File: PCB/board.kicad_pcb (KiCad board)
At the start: 2 copper layers, 81.7 x 88.8 mm, 161 parts, among them J1 Micro_SD_Card, J10 Conn_01x10, J11 Conn_01x02, J12 Conn_02x04_Odd_Even, J13 Conn_01x02, J14 Conn_01x02, J15 Conn_01x03, J16 Conn_01x02, J17 Conn_01x05, J18 Conn_01x04, J19 Conn_01x04, J2 Conn_ARM_JTAG_SWD_10, J20 Conn_01x02, J21 Conn_01x03, J22 Conn_02x04_Odd_Even, J23 Conn_01x04, J24 Conn_01x04, J25 Conn_01x02, J26 Conn_01x03, J27 Conn_02x04_Odd_Even, J28 Conn_01x04, J29 Conn_01x04, J3 USB_C_Receptacle_USB2.0_14P, J30 Conn_01x02, J31 Conn_01x03, J32 Conn_01x02, J33 Conn_01x02, J34 Conn_01x02, J35 Conn_01x02, J36 Conn_01x02, J37 Conn_01x02, J4 Conn_01x04, J5 Conn_01x04, J6 Conn_01x02, J7 Conn_01x03, J8 Conn_02x04_Odd_Even, J9 Conn_01x10, Q1 IRLML6402, Q2 NMOS, Q3 NMOS, Q4 NMOS, Q5 Q_NMOS_GDS, Q7 Q_NMOS_GDS, SW1 SW_Push, SW2 SW_Push, U1 STM32H743VITx, U2 AP7361C, U4 TMC Stepstick, U5 TMC Stepstick, U6 TMC Stepstick, U7 TMC Stepstick, U8 AP63203WU, Y2 25 MHz

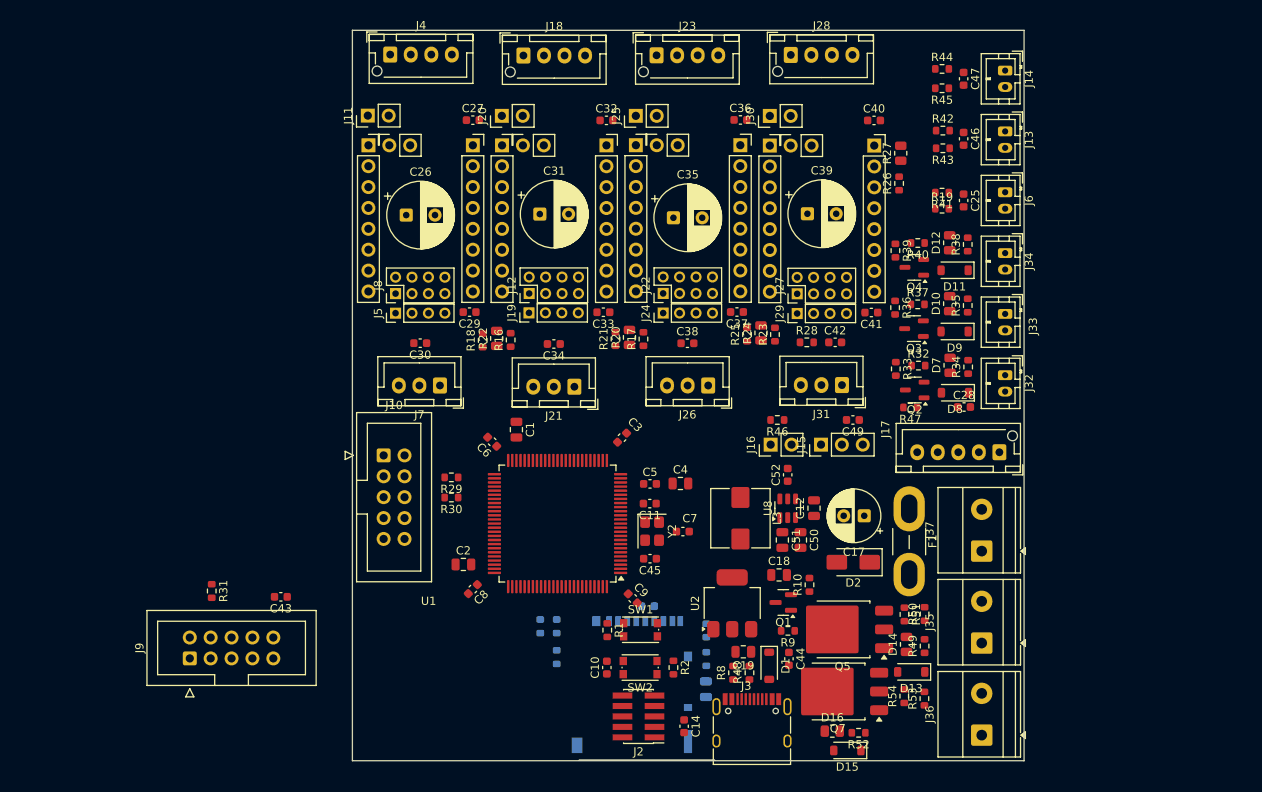
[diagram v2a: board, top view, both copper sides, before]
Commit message: first round of mounting holes
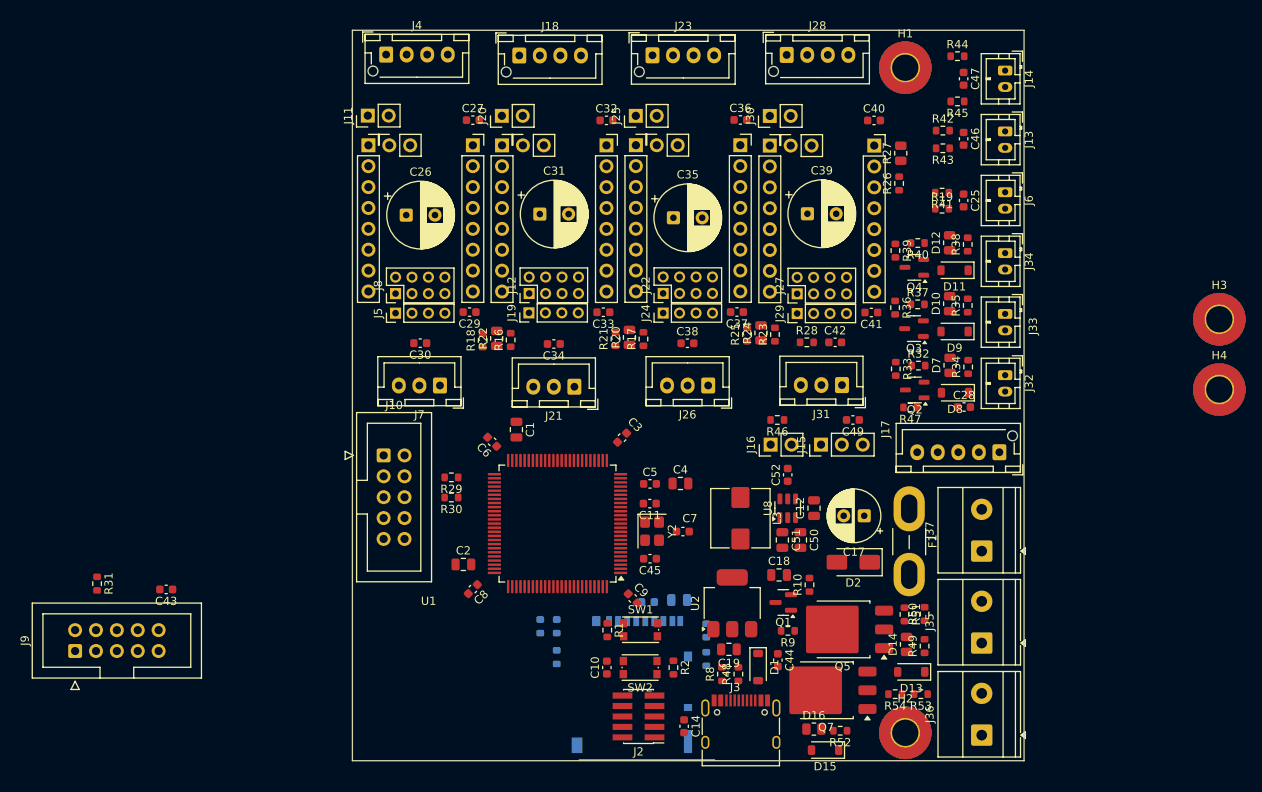
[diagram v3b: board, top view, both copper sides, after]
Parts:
- added H1: MountingHole_Pad, MountingHole:MountingHole_3.2mm_M3_Pad_TopBottom, F.Cu at (220.8, 28.5)
- added H2: MountingHole_Pad, MountingHole:MountingHole_3.2mm_M3_Pad_TopBottom, F.Cu at (220.8, 109.4)
- added H3: MountingHole_Pad, MountingHole:MountingHole_3.2mm_M3_Pad_TopBottom, F.Cu at (259.0, 59.1)
- added H4: MountingHole_Pad, MountingHole:MountingHole_3.2mm_M3_Pad_TopBottom, F.Cu at (259.0, 67.7)
- moved J9 14.0 mm to (119.8, 99.5)
- moved R31 14.0 mm to (122.5, 91.3)
- moved C43 14.0 mm to (130.9, 92.0)
- moved C16 11.3 mm to (193.3, 93.2), turned to 0 degrees
- moved D15 2.70 mm to (211.1, 111.5)
- moved R45 2.46 mm to (227.2, 32.6)
- moved R44 2.43 mm to (227.2, 27.1)
- moved D16 2.25 mm to (209.7, 109.0)
- moved R52 2.25 mm to (212.9, 109.2)
- moved C19 1.78 mm to (199.3, 99.2)
- moved Q7 1.43 mm to (211.2, 104.2)
- moved J3 1.36 mm to (200.8, 109.5)
- moved R48 1.36 mm to (200.5, 102.3)
- moved R8 1.36 mm to (198.5, 102.3)
- moved C44 1.36 mm to (205.3, 100.6)
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
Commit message: ALL mounting holes placed down
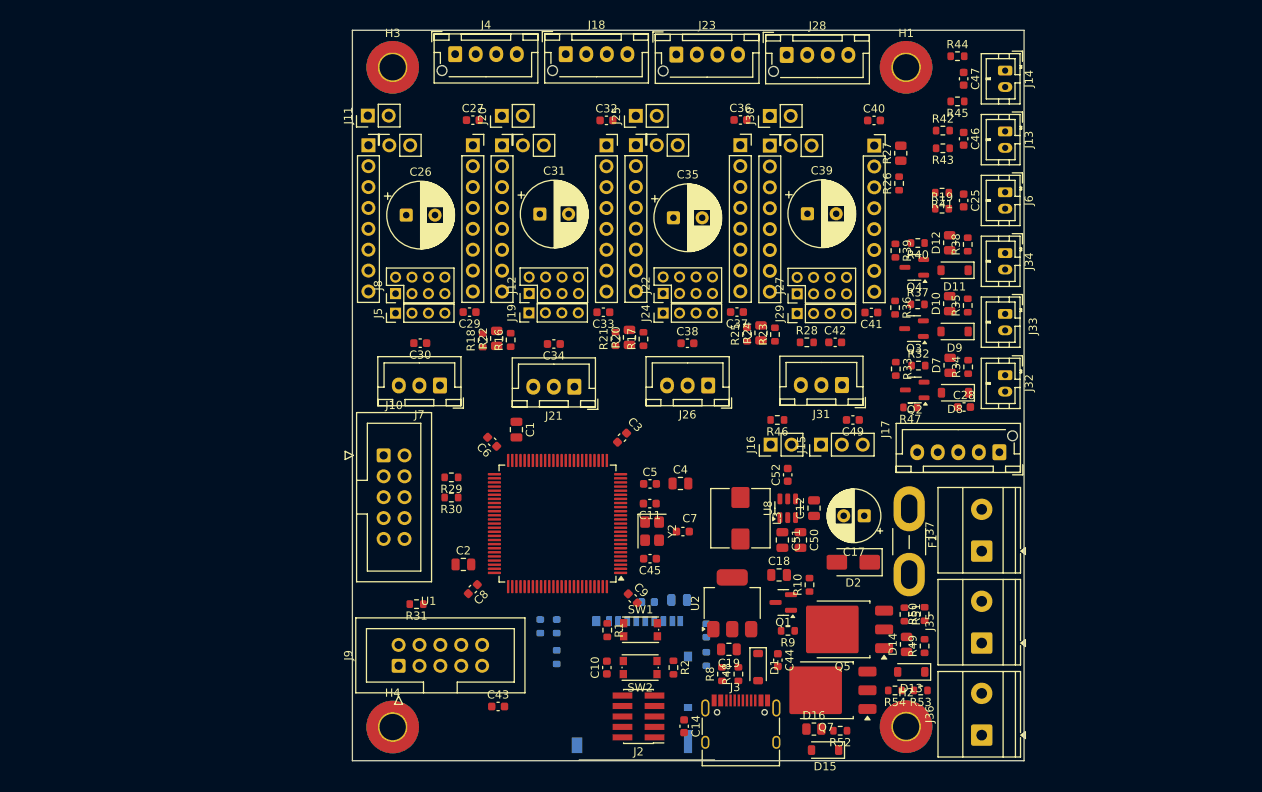
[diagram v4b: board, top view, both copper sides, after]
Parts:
- moved H4 108.6 mm to (158.4, 108.7)
- moved H3 105.1 mm to (158.4, 28.4)
- moved C43 42.8 mm to (171.3, 106.2), turned to 0 degrees
- moved J9 39.4 mm to (159.2, 101.3)
- moved R31 38.9 mm to (161.3, 93.8), turned to 180 degrees
- moved J4 8.40 mm to (166.1, 26.9)
- moved J18 5.65 mm to (179.5, 26.9)
- moved J23 2.90 mm to (192.9, 26.9)
- moved H2 0.76 mm to (220.9, 108.7)
- moved R53 0.45 mm to (222.7, 104.2)
- moved R54 0.45 mm to (219.6, 104.2)
- moved H1 0.11 mm to (220.9, 28.4)
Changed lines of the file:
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@@
 	(footprint "Connector_JST:JST_XH_B4B-XH-AM_1x04_P2.50mm_Vertical"
 		(layer "F.Cu")
-		(at 157.65 26.90375)
+		(at 166.05 26.85)
 		(descr "JST XH series connector, B4B-XH-AM, with boss (http://www.jst-mfg.com/product/pdf/eng/eXH.pdf), generated with kicad-footprint-generator")
 		(tags "connector JST XH vertical boss")
@@
 	(footprint "MountingHole:MountingHole_3.2mm_M3_Pad_TopBottom"
 		(layer "F.Cu")
-		(at 259 59.1)
+		(at 158.45 28.45)
 		(descr "Mounting Hole 3.2mm, M3, generated by kicad-footprint-generator mountinghole.py")
 		(tags "mountinghole M3")
@@
 	(footprint "MountingHole:MountingHole_3.2mm_M3_Pad_TopBottom"
 		(layer "F.Cu")
-		(at 259 67.65)
+		(at 158.45 108.7)
 		(descr "Mounting Hole 3.2mm, M3, generated by kicad-footprint-generator mountinghole.py")
 		(tags "mountinghole M3")
@@
 	(footprint "Capacitor_SMD:C_0603_1608Metric"
 		(layer "F.Cu")
-		(at 130.9 91.9625 180)
+		(at 171.275 106.2)
 		(descr "Capacitor SMD 0603 (1608 Metric), square (rectangular) end terminal, IPC-7351 nominal, (Body size source: IPC-SM-782 page 76, https://www.pcb-3d.com/wordpress/wp-content/uploads/ipc-sm-782a_amendment_1_and_2.pdf), generated with kicad-footprint-generator")
 		(tags "capacitor")
@@
 		(attr smd)
 		(fp_line
-			(start -0.14058 0.51)
-			(end 0.14058 0.51)
+			(start -0.14058 -0.51)
+			(end 0.14058 -0.51)
 			(stroke
 				(width 0.12)
@@
 		)
 		(fp_line
-			(start -0.14058 -0.51)
-			(end 0.14058 -0.51)
+			(start -0.14058 0.51)
+			(end 0.14058 0.51)
 			(stroke
 				(width 0.12)
@@
 		)
 		(fp_line
-			(start 1.48 0.73)
-			(end -1.48 0.73)
+			(start -1.48 -0.73)
+			(end 1.48 -0.73)
 			(stroke
 				(width 0.05)
@@
 		)
 		(fp_line
-			(start 1.48 -0.73)
-			(end 1.48 0.73)
+			(start -1.48 0.73)
+			(end -1.48 -0.73)
 			(stroke
 				(width 0.05)
@@
 		)
 		(fp_line
-			(start -1.48 0.73)
-			(end -1.48 -0.73)
+			(start 1.48 -0.73)
+			(end 1.48 0.73)
 			(stroke
 				(width 0.05)
@@
 		)
 		(fp_line
-			(start -1.48 -0.73)
-			(end 1.48 -0.73)
+			(start 1.48 0.73)
+			(end -1.48 0.73)
 			(stroke
 				(width 0.05)
@@
 		)
 		(fp_line
-			(start 0.8 0.4)
-			(end -0.8 0.4)
+			(start -0.8 -0.4)
+			(end 0.8 -0.4)
 			(stroke
 				(width 0.1)
@@
 		)
 		(fp_line
-			(start 0.8 -0.4)
-			(end 0.8 0.4)
+			(start -0.8 0.4)
+			(end -0.8 -0.4)
 			(stroke
 				(width 0.1)
@@
 		)
 		(fp_line
-			(start -0.8 0.4)
-			(end -0.8 -0.4)
+			(start 0.8 -0.4)
+			(end 0.8 0.4)
 			(stroke
 				(width 0.1)
@@
 		)
 		(fp_line
-			(start -0.8 -0.4)
-			(end 0.8 -0.4)
+			(start 0.8 0.4)
+			(end -0.8 0.4)
 			(stroke
 				(width 0.1)
@@
 		)
 		(pad "1" smd roundrect
-			(at -0.775 0 180)
+			(at -0.775 0)
 			(size 0.9 0.95)
 			(layers "F.Cu" "F.Mask" "F.Paste")
@@
 		)
 		(pad "2" smd roundrect
-			(at 0.775 0 180)
+			(at 0.775 0)
 			(size 0.9 0.95)
 			(layers "F.Cu" "F.Mask" "F.Paste")
@@
 	(footprint "MountingHole:MountingHole_3.2mm_M3_Pad_TopBottom"
 		(layer "F.Cu")
-		(at 220.8 109.4)
+		(at 220.9 108.65)
 		(descr "Mounting Hole 3.2mm, M3, generated by kicad-footprint-generator mountinghole.py")
 		(tags "mountinghole M3")
@@
 	(footprint "Resistor_SMD:R_0603_1608Metric"
 		(layer "F.Cu")
-		(at 122.49 91.2525 -90)
+		(at 161.35 93.75 180)
 		(descr "Resistor SMD 0603 (1608 Metric), square (rectangular) end terminal, IPC-7351 nominal, (Body size source: IPC-SM-782 page 72, https://www.pcb-3d.com/wordpress/wp-content/uploads/ipc-sm-782a_amendment_1_and_2.pdf), generated with kicad-footprint-generator")
 		(tags "resistor")
 		(property "Reference" "R31"
-			(at 0 -1.43 90)
+			(at 0 -1.43 0)
 			(layer "F.SilkS")
 			(effects
@@
 		)
 		(property "Value" "10K"
-			(at 0 1.43 90)
+			(at 0 1.43 0)
 			(layer "F.Fab")
 			(effects
@@
 		)
 		(property "Datasheet" "~"
-			(at 0 0 90)
+			(at 0 0 0)
 			(layer "F.Fab")
 			(hide yes)
@@
 		)
 		(property "Description" "Resistor"
-			(at 0 0 90)
+			(at 0 0 0)
 			(layer "F.Fab")
 			(hide yes)
@@
 		)
 		(fp_line
-			(start -1.48 0.73)
-			(end -1.48 -0.73)
+			(start 1.48 0.73)
+			(end -1.48 0.73)
 			(stroke
 				(width 0.05)
@@
 		)
 		(fp_line
-			(start 1.48 0.73)
-			(end -1.48 0.73)
+			(start 1.48 -0.73)
+			(end 1.48 0.73)
 			(stroke
 				(width 0.05)
@@
 		)
 		(fp_line
-			(start -1.48 -0.73)
-			(end 1.48 -0.73)
+			(start -1.48 0.73)
+			(end -1.48 -0.73)
 			(stroke
 				(width 0.05)
@@
 		)
 		(fp_line
-			(start 1.48 -0.73)
-			(end 1.48 0.73)
+			(start -1.48 -0.73)
+			(end 1.48 -0.73)
 			(stroke
 				(width 0.05)
@@
 		)
 		(fp_line
-			(start -0.8 0.4125)
-			(end -0.8 -0.4125)
+			(start 0.8 0.4125)
+			(end -0.8 0.4125)
 			(stroke
 				(width 0.1)
@@
 		)
 		(fp_line
-			(start 0.8 0.4125)
-			(end -0.8 0.4125)
+			(start 0.8 -0.4125)
+			(end 0.8 0.4125)
 			(stroke
 				(width 0.1)
@@
 		)
 		(fp_line
-			(start -0.8 -0.4125)
-			(end 0.8 -0.4125)
+			(start -0.8 0.4125)
+			(end -0.8 -0.4125)
 			(stroke
 				(width 0.1)
@@
 		)
 		(fp_line
-			(start 0.8 -0.4125)
-			(end 0.8 0.4125)
+			(start -0.8 -0.4125)
+			(end 0.8 -0.4125)
 			(stroke
 				(width 0.1)
@@
 		)
 		(fp_text user "${REFERENCE}"
-			(at 0 0 90)
+			(at 0 0 0)
 			(layer "F.Fab")
 			(effects
@@
 		)
 		(pad "1" smd roundrect
-			(at -0.825 0 270)
+			(at -0.825 0 180)
 			(size 0.8 0.95)
 			(layers "F.Cu" "F.Mask" "F.Paste")
@@
 		)
 		(pad "2" smd roundrect
-			(at 0.825 0 270)
+			(at 0.825 0 180)
 			(size 0.8 0.95)
 			(layers "F.Cu" "F.Mask" "F.Paste")
@@
 	(footprint "Connector_IDC:IDC-Header_2x05_P2.54mm_Vertical"
 		(layer "F.Cu")
-		(at 119.82 99.4525 90)
+		(at 159.17 101.2525 90)
 		(descr "Through hole IDC box header, 2x05, 2.54mm pitch, DIN 41651 / IEC 60603-13, double rows, https://docs.google.com/spreadsheets/d/16SsEcesNF15N3Lb4niX7dcUr-NY5_MFPQhobNuNppn4/edit#gid=0")
 		(tags "Through hole vertical IDC box header THT 2x05 2.54mm double row")
@@
 	(footprint "Resistor_SMD:R_0603_1608Metric"
 		(layer "F.Cu")
-		(at 222.7 104.7 180)
+		(at 222.675 104.25 180)
 		(descr "Resistor SMD 0603 (1608 Metric), square (rectangular) end terminal, IPC-7351 nominal, (Body size source: IPC-SM-782 page 72, https://www.pcb-3d.com/wordpress/wp-content/uploads/ipc-sm-782a_amendment_1_and_2.pdf), generated with kicad-footprint-generator")
 		(tags "resistor")
@@
 	(footprint "Resistor_SMD:R_0603_1608Metric"
 		(layer "F.Cu")
-		(at 219.575 104.7 180)
+		(at 219.55 104.25 180)
 		(descr "Resistor SMD 0603 (1608 Metric), square (rectangular) end terminal, IPC-7351 nominal, (Body size source: IPC-SM-782 page 72, https://www.pcb-3d.com/wordpress/wp-content/uploads/ipc-sm-782a_amendment_1_and_2.pdf), generated with kicad-footprint-generator")
 		(tags "resistor")
@@
 	(footprint "Connector_JST:JST_XH_B4B-XH-AM_1x04_P2.50mm_Vertical"
 		(layer "F.Cu")
-		(at 173.852651 27.01875)
+		(at 179.5 26.85)
 		(descr "JST XH series connector, B4B-XH-AM, with boss (http://www.jst-mfg.com/product/pdf/eng/eXH.pdf), generated with kicad-footprint-generator")
 		(tags "connector JST XH vertical boss")
@@
 	(footprint "MountingHole:MountingHole_3.2mm_M3_Pad_TopBottom"
 		(layer "F.Cu")
-		(at 220.8 28.5)
+		(at 220.9 28.45)
 		(descr "Mounting Hole 3.2mm, M3, generated by kicad-footprint-generator mountinghole.py")
 		(tags "mountinghole M3")
@@
 	(footprint "Connector_JST:JST_XH_B4B-XH-AM_1x04_P2.50mm_Vertical"
 		(layer "F.Cu")
-		(at 190.05 26.99375)
+		(at 192.95 26.9)
 		(descr "JST XH series connector, B4B-XH-AM, with boss (http://www.jst-mfg.com/product/pdf/eng/eXH.pdf), generated with kicad-footprint-generator")
 		(tags "connector JST XH vertical boss")

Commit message: fine tuning some stuff
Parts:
- moved C15 0.32 mm to (189.6, 93.8)
- moved C16 0.32 mm to (193.4, 93.5)
- moved J1 0.32 mm to (187.7, 103.8)
- moved R3 0.32 mm to (176.5, 96.8)
- moved R4 0.32 mm to (178.5, 96.8)
- moved R5 0.32 mm to (178.5, 100.5)
- moved R6 0.32 mm to (196.7, 100.7)
- moved R7 0.32 mm to (196.7, 97.2)
- moved J9 0.13 mm to (159.3, 101.2)
- moved C43 0.13 mm to (171.4, 106.2)
- moved R31 0.13 mm to (161.5, 93.7)
- moved J31 0.10 mm to (213.1, 67.0)
- moved C41 0.10 mm to (216.7, 58.2)
- moved J27 0.10 mm to (207.7, 55.9)
- moved J30 0.10 mm to (204.3, 34.3)
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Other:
- board size 81.7 x 88.8 mm -> 81.6 x 88.8 mm
